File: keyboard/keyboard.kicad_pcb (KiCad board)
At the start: 2 copper layers, 214.3 x 133.3 mm, 131 parts, among them SW1 MX_SW_HS, SW10 MX_SW_HS, SW11 MX_SW_HS, SW12 MX_SW_HS, SW13 MX_SW_HS, SW14 MX_SW_HS, SW15 MX_SW_HS, SW16 MX_SW_HS, SW17 MX_SW_HS, SW18 MX_SW_HS, SW19 MX_SW_HS, SW2 MX_SW_HS, SW20 MX_SW_HS, SW21 MX_SW_HS, SW22 MX_SW_HS, SW23 MX_SW_HS, SW24 MX_SW_HS, SW25 MX_SW_HS, SW26 MX_SW_HS, SW27 MX_SW_HS, SW28 MX_SW_HS, SW29 MX_SW_HS, SW3 MX_SW_HS, SW30 MX_SW_HS, SW31 MX_SW_HS, SW32 MX_SW_HS, SW33 MX_SW_HS, SW34 MX_SW_HS, SW35 MX_SW_HS, SW36 MX_SW_HS, SW37 MX_SW_HS, SW38 MX_SW_HS, SW39 MX_SW_HS, SW4 MX_SW_HS, SW40 MX_SW_HS, SW41 MX_SW_HS, SW42 MX_SW_HS, SW43 MX_SW_HS, SW44 MX_SW_HS, SW45 MX_SW_HS, SW46 MX_SW_HS, SW47 MX_SW_HS, SW48 MX_SW_HS, SW49 MX_SW_HS, SW5 MX_SW_HS, SW50 MX_SW_HS, SW51 MX_SW_HS, SW52 MX_SW_HS, SW53 MX_SW_HS, SW54 MX_SW_HS, SW55 MX_SW_HS, SW56 MX_SW_HS, SW57 MX_SW_HS, SW58 MX_SW_HS, SW59 MX_SW_HS, SW6 MX_SW_HS, SW60 MX_SW_HS, SW61 MX_SW_HS, SW62 MX_SW_HS, SW63 MX_SW_HS, SW64 MX_SW_HS, SW7 MX_SW_HS, SW8 MX_SW_HS, SW9 MX_SW_HS, U1 ProMicro

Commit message: Update the PCB with the wiring for the rows and columns
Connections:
- D1 pad 1: unconnected-(D1-Pad1) -> ROW0
- D10 pad 1: unconnected-(D10-Pad1) -> ROW0
- D11 pad 1: unconnected-(D11-Pad1) -> ROW7
- D12 pad 1: unconnected-(D12-Pad1) -> ROW0
- D13 pad 1: unconnected-(D13-Pad1) -> ROW1
- D14 pad 1: unconnected-(D14-Pad1) -> ROW2
- D15 pad 1: unconnected-(D15-Pad1) -> ROW3
- D16 pad 1: unconnected-(D16-Pad1) -> ROW4
- D17 pad 1: unconnected-(D17-Pad1) -> ROW5
- D18 pad 1: unconnected-(D18-Pad1) -> ROW6
- D19 pad 1: unconnected-(D19-Pad1) -> ROW7
- D2 pad 1: unconnected-(D2-Pad1) -> ROW1
- D20 pad 1: unconnected-(D20-Pad1) -> ROW1
- D21 pad 1: unconnected-(D21-Pad1) -> ROW1
- D22 pad 1: unconnected-(D22-Pad1) -> ROW6
- D23 pad 1: unconnected-(D23-Pad1) -> ROW0
- D24 pad 1: unconnected-(D24-Pad1) -> ROW1
- D25 pad 1: unconnected-(D25-Pad1) -> ROW2
- D26 pad 1: unconnected-(D26-Pad1) -> ROW3
- D27 pad 1: unconnected-(D27-Pad1) -> ROW4
- D28 pad 1: unconnected-(D28-Pad1) -> ROW5
- D29 pad 1: unconnected-(D29-Pad1) -> ROW6
- D3 pad 1: unconnected-(D3-Pad1) -> ROW2
- D30 pad 1: unconnected-(D30-Pad1) -> ROW7
- D31 pad 1: unconnected-(D31-Pad1) -> ROW2
- D32 pad 1: unconnected-(D32-Pad1) -> ROW2
- D33 pad 1: unconnected-(D33-Pad1) -> ROW5
- D34 pad 1: unconnected-(D34-Pad1) -> ROW0
- D35 pad 1: unconnected-(D35-Pad1) -> ROW1
- D36 pad 1: unconnected-(D36-Pad1) -> ROW2
- D37 pad 1: unconnected-(D37-Pad1) -> ROW3
- D38 pad 1: unconnected-(D38-Pad1) -> ROW4
- D39 pad 1: unconnected-(D39-Pad1) -> ROW5
- D4 pad 1: unconnected-(D4-Pad1) -> ROW3
- D40 pad 1: unconnected-(D40-Pad1) -> ROW6
- D41 pad 1: unconnected-(D41-Pad1) -> ROW7
- D42 pad 1: unconnected-(D42-Pad1) -> ROW3
- D43 pad 1: unconnected-(D43-Pad1) -> ROW3
- D44 pad 1: unconnected-(D44-Pad1) -> ROW4
- D45 pad 1: unconnected-(D45-Pad1) -> ROW0
- D46 pad 1: unconnected-(D46-Pad1) -> ROW1
- D47 pad 1: unconnected-(D47-Pad1) -> ROW2
- D48 pad 1: unconnected-(D48-Pad1) -> ROW3
- D49 pad 1: unconnected-(D49-Pad1) -> ROW4
- D5 pad 1: unconnected-(D5-Pad1) -> ROW4
- D50 pad 1: unconnected-(D50-Pad1) -> ROW5
- D51 pad 1: unconnected-(D51-Pad1) -> ROW6
- D52 pad 1: unconnected-(D52-Pad1) -> ROW7
- D53 pad 1: unconnected-(D53-Pad1) -> ROW4
- D54 pad 1: unconnected-(D54-Pad1) -> ROW7
- D55 pad 1: unconnected-(D55-Pad1) -> ROW0
- D56 pad 1: unconnected-(D56-Pad1) -> ROW1
- D57 pad 1: unconnected-(D57-Pad1) -> ROW2
- D58 pad 1: unconnected-(D58-Pad1) -> ROW3
- D59 pad 1: unconnected-(D59-Pad1) -> ROW4
- D6 pad 1: unconnected-(D6-Pad1) -> ROW5
- D60 pad 1: unconnected-(D60-Pad1) -> ROW5
- D61 pad 1: unconnected-(D61-Pad1) -> ROW6
- D62 pad 1: unconnected-(D62-Pad1) -> ROW7
- D63 pad 1: unconnected-(D63-Pad1) -> ROW5
- D64 pad 1: unconnected-(D64-Pad1) -> ROW6
- D7 pad 1: unconnected-(D7-Pad1) -> ROW6
- D8 pad 1: unconnected-(D8-Pad1) -> ROW7
- D9 pad 1: unconnected-(D9-Pad1) -> ROW0
- SW1 pad 2: unconnected-(SW1-Pad2) -> COL0
- SW10 pad 2: unconnected-(SW10-Pad2) -> COL7
- SW11 pad 2: unconnected-(SW11-Pad2) -> COL7
- SW12 pad 2: unconnected-(SW12-Pad2) -> COL1
- SW13 pad 2: unconnected-(SW13-Pad2) -> COL1
- SW14 pad 2: unconnected-(SW14-Pad2) -> COL1
- SW15 pad 2: unconnected-(SW15-Pad2) -> COL1
- SW16 pad 2: unconnected-(SW16-Pad2) -> COL1
- SW17 pad 2: unconnected-(SW17-Pad2) -> COL1
- SW18 pad 2: unconnected-(SW18-Pad2) -> COL1
- SW19 pad 2: unconnected-(SW19-Pad2) -> COL1
- SW2 pad 2: unconnected-(SW2-Pad2) -> COL0
- SW20 pad 2: unconnected-(SW20-Pad2) -> COL6
- SW21 pad 2: unconnected-(SW21-Pad2) -> COL7
- SW22 pad 2: unconnected-(SW22-Pad2) -> COL7
- SW23 pad 2: unconnected-(SW23-Pad2) -> COL2
- SW24 pad 2: unconnected-(SW24-Pad2) -> COL2
- SW25 pad 2: unconnected-(SW25-Pad2) -> COL2
- SW26 pad 2: unconnected-(SW26-Pad2) -> COL2
- SW27 pad 2: unconnected-(SW27-Pad2) -> COL2
- SW28 pad 2: unconnected-(SW28-Pad2) -> COL2
- SW29 pad 2: unconnected-(SW29-Pad2) -> COL2
- SW3 pad 2: unconnected-(SW3-Pad2) -> COL0
- SW30 pad 2: unconnected-(SW30-Pad2) -> COL2
- SW31 pad 2: unconnected-(SW31-Pad2) -> COL6
- SW32 pad 2: unconnected-(SW32-Pad2) -> COL7
- SW33 pad 2: unconnected-(SW33-Pad2) -> COL7
- SW34 pad 2: unconnected-(SW34-Pad2) -> COL3
- SW35 pad 2: unconnected-(SW35-Pad2) -> COL3
- SW36 pad 2: unconnected-(SW36-Pad2) -> COL3
- SW37 pad 2: unconnected-(SW37-Pad2) -> COL3
- SW38 pad 2: unconnected-(SW38-Pad2) -> COL3
- SW39 pad 2: unconnected-(SW39-Pad2) -> COL3
- SW4 pad 2: unconnected-(SW4-Pad2) -> COL0
- SW40 pad 2: unconnected-(SW40-Pad2) -> COL3
- SW41 pad 2: unconnected-(SW41-Pad2) -> COL3
- SW42 pad 2: unconnected-(SW42-Pad2) -> COL6
- SW43 pad 2: unconnected-(SW43-Pad2) -> COL7
- SW44 pad 2: unconnected-(SW44-Pad2) -> COL7
- SW45 pad 2: unconnected-(SW45-Pad2) -> COL4
- SW46 pad 2: unconnected-(SW46-Pad2) -> COL4
- SW47 pad 2: unconnected-(SW47-Pad2) -> COL4
- SW48 pad 2: unconnected-(SW48-Pad2) -> COL4
- SW49 pad 2: unconnected-(SW49-Pad2) -> COL4
- SW5 pad 2: unconnected-(SW5-Pad2) -> COL0
- SW50 pad 2: unconnected-(SW50-Pad2) -> COL4
- SW51 pad 2: unconnected-(SW51-Pad2) -> COL4
- SW52 pad 2: unconnected-(SW52-Pad2) -> COL4
- SW53 pad 2: unconnected-(SW53-Pad2) -> COL6
- SW54 pad 2: unconnected-(SW54-Pad2) -> COL6
- SW55 pad 2: unconnected-(SW55-Pad2) -> COL5
- SW56 pad 2: unconnected-(SW56-Pad2) -> COL5
- SW57 pad 2: unconnected-(SW57-Pad2) -> COL5
- SW58 pad 2: unconnected-(SW58-Pad2) -> COL5
- SW59 pad 2: unconnected-(SW59-Pad2) -> COL5
- SW6 pad 2: unconnected-(SW6-Pad2) -> COL0
- SW60 pad 2: unconnected-(SW60-Pad2) -> COL5
- SW61 pad 2: unconnected-(SW61-Pad2) -> COL5
- SW62 pad 2: unconnected-(SW62-Pad2) -> COL5
- SW63 pad 2: unconnected-(SW63-Pad2) -> COL6
- SW64 pad 2: unconnected-(SW64-Pad2) -> COL6
- SW7 pad 2: unconnected-(SW7-Pad2) -> COL0
- SW8 pad 2: unconnected-(SW8-Pad2) -> COL0
- SW9 pad 2: unconnected-(SW9-Pad2) -> COL6

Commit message: Start to add the wiring for the keyboard
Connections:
- net RESET renamed RST
- RESET1 pad 1: unconnected-(RESET1-Pad1) -> GND
- U1 pad 1: unconnected-(U1-Pad1) -> ROW0
- U1 pad 10: unconnected-(U1-Pad10) -> ROW5
- U1 pad 11: unconnected-(U1-Pad11) -> ROW6
- U1 pad 12: unconnected-(U1-Pad12) -> ROW7
- U1 pad 13: unconnected-(U1-Pad13) -> COL7
- U1 pad 14: unconnected-(U1-Pad14) -> COL6
- U1 pad 15: unconnected-(U1-Pad15) -> COL5
- U1 pad 16: unconnected-(U1-Pad16) -> COL4
- U1 pad 17: unconnected-(U1-Pad17) -> COL3
- U1 pad 18: unconnected-(U1-Pad18) -> COL2
- U1 pad 19: unconnected-(U1-Pad19) -> COL1
- U1 pad 2: unconnected-(U1-Pad2) -> ROW1
- U1 pad 20: unconnected-(U1-Pad20) -> COL0
- U1 pad 21: unconnected-(U1-Pad21) -> VCC
- U1 pad 23: unconnected-(U1-Pad23) -> GND
- U1 pad 24: unconnected-(U1-Pad24) -> RAW
- U1 pad 3: unconnected-(U1-Pad3) -> GND
- U1 pad 4: unconnected-(U1-Pad4) -> GND
- U1 pad 5: unconnected-(U1-Pad5) -> SDA
- U1 pad 6: unconnected-(U1-Pad6) -> SCL
- U1 pad 7: unconnected-(U1-Pad7) -> ROW2
- U1 pad 8: unconnected-(U1-Pad8) -> ROW3
- U1 pad 9: unconnected-(U1-Pad9) -> ROW4

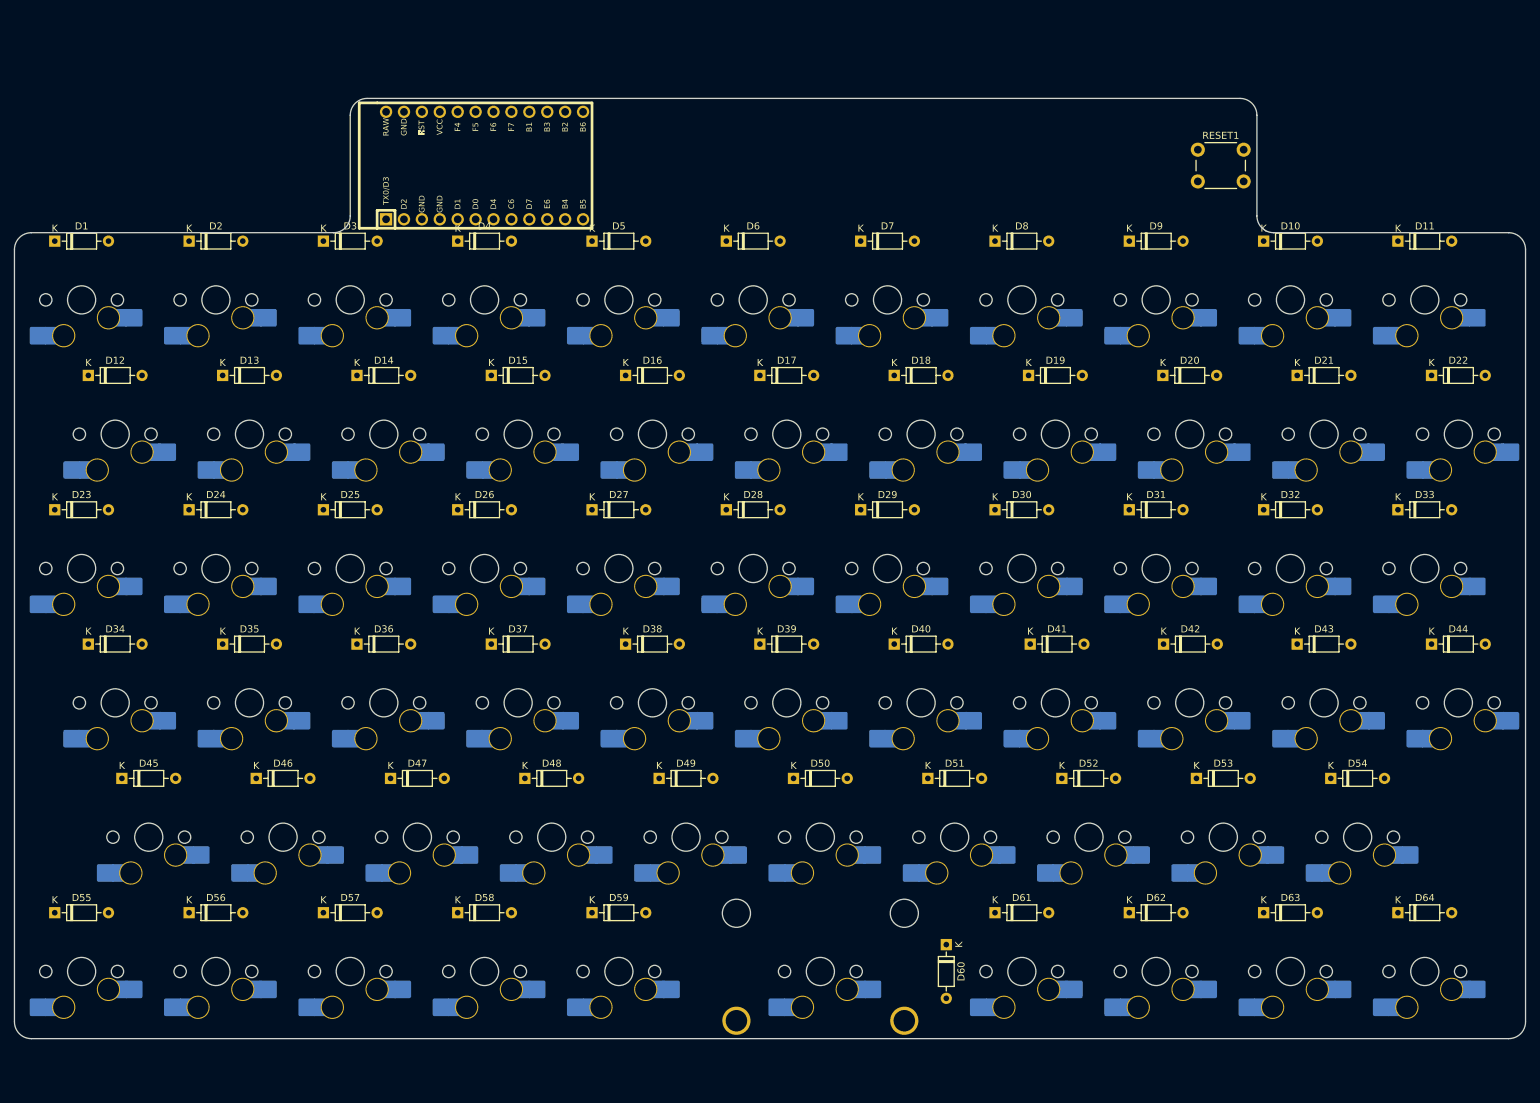
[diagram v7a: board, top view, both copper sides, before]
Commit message: Add the power and clean up the reset button a little
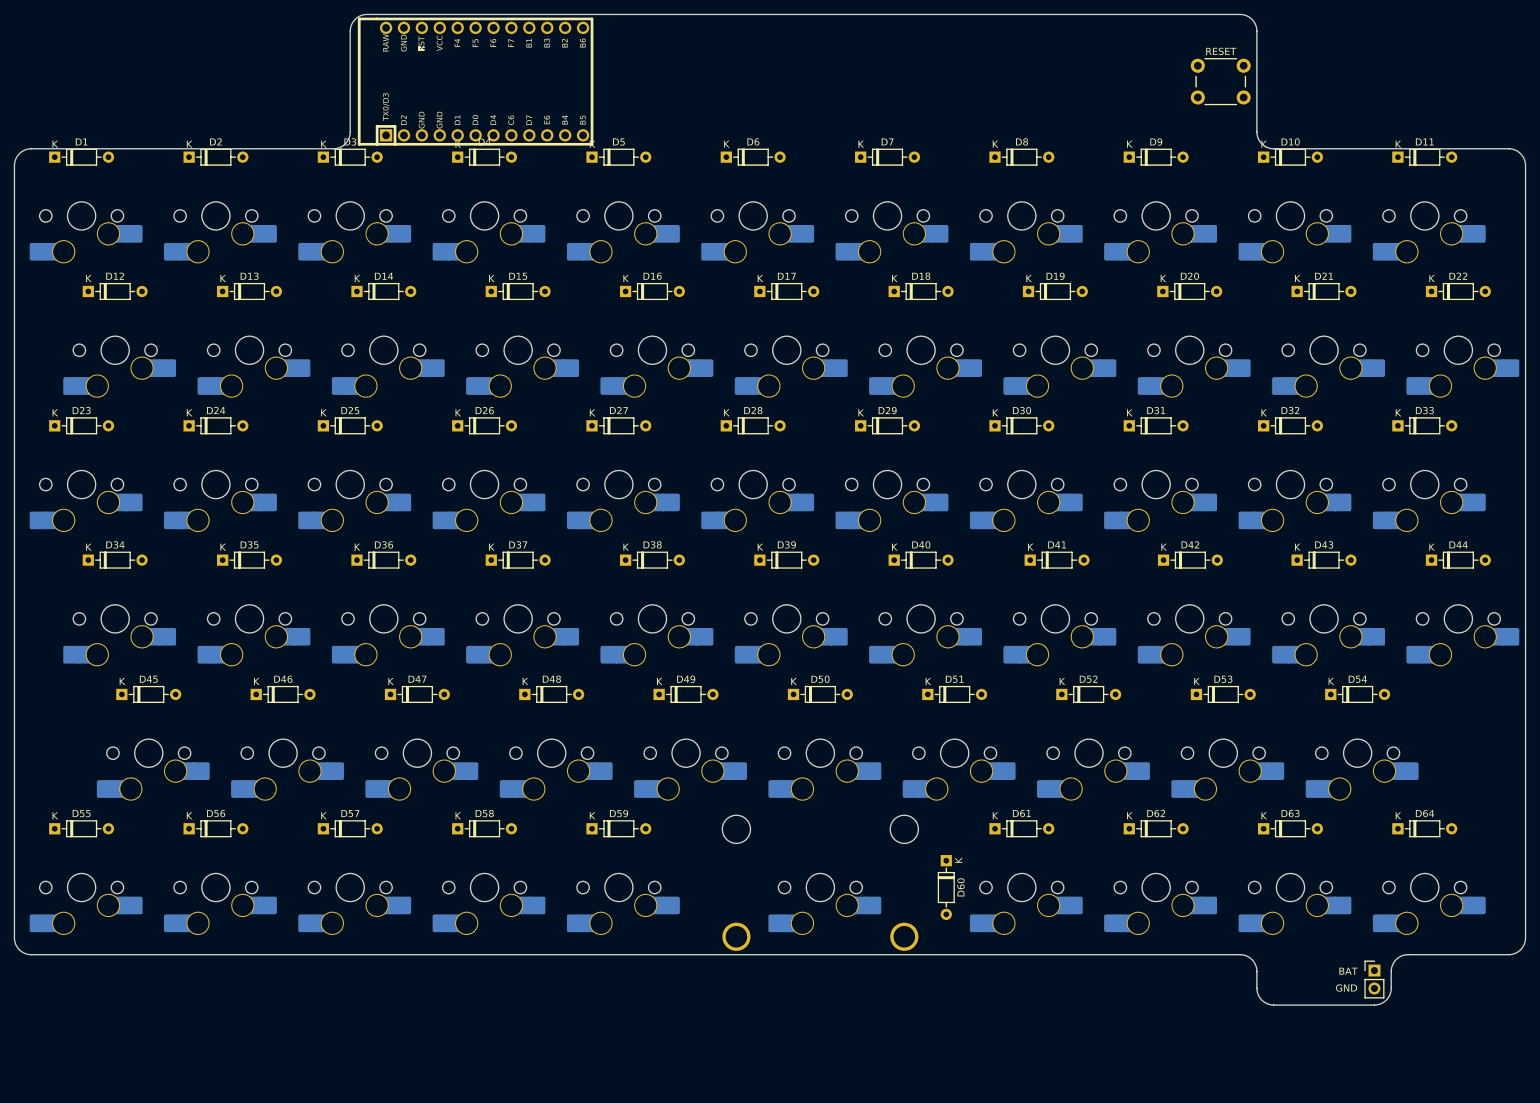
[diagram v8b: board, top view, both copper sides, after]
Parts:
- added POWER1: Conn_01x02_Male, Connector_PinHeader_2.54mm:PinHeader_1x02_P2.54mm_Vertical, F.Cu at (233.4, 149.9)
- moved D1 11.9 mm to (46.2, 34.5)
- moved D10 11.9 mm to (217.6, 34.5)
- moved D11 11.9 mm to (236.7, 34.5)
- moved D12 11.9 mm to (51.0, 53.6)
- moved D13 11.9 mm to (70.0, 53.6)
- moved D14 11.9 mm to (89.1, 53.6)
- moved D15 11.9 mm to (108.1, 53.6)
- moved D16 11.9 mm to (127.2, 53.6)
- moved D17 11.9 mm to (146.2, 53.6)
- moved D18 11.9 mm to (165.3, 53.6)
- moved D19 11.9 mm to (184.3, 53.6)
- moved D2 11.9 mm to (65.2, 34.5)
- moved D20 11.9 mm to (203.4, 53.6)
- moved D21 11.9 mm to (222.4, 53.6)
- moved D22 11.9 mm to (241.5, 53.6)
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- renumbered RESET1 to RESET
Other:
- board size 214.3 x 133.3 mm -> 214.3 x 140.5 mm
- board text added: "BAT"
- board text added: "GND"
